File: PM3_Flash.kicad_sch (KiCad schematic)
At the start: 4 parts, among them J1 Conn_01x02, J2 Conn_01x04, U1 W25Qxx

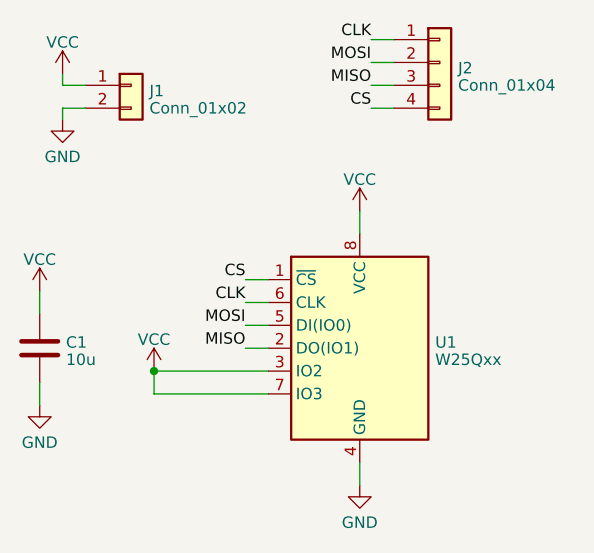
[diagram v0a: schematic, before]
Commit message: 10uF->100nF
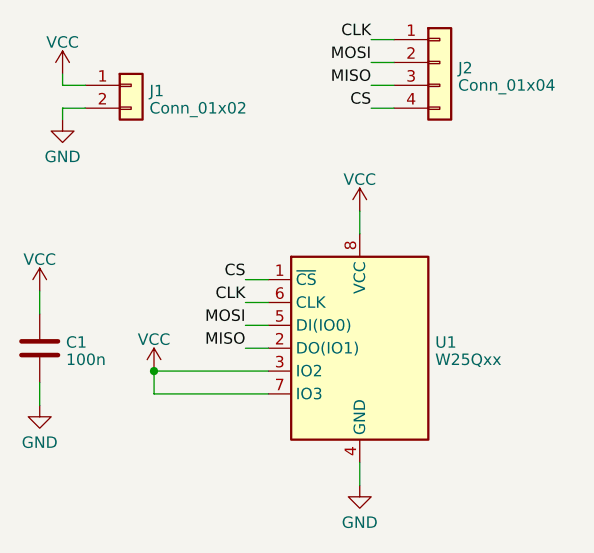
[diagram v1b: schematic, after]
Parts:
- C1: value 10u -> 100n
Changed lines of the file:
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@@
       (effects (font (size 1.27 1.27)) (justify left))
     )
-    (property "Value" "10u" (at 103.251 93.9873 0)
+    (property "Value" "100n" (at 103.251 93.9873 0)
       (effects (font (size 1.27 1.27)) (justify left))
     )
